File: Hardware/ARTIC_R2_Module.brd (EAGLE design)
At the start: 20.3 x 33 mm, 144 parts, among them J25 U.FL, K1 TLP3475R, Q2 5.8A/30V/35mΩ, U1 ADM4210-1, U2 1.8V/100mA, U3 ARTIC_R2, U4 RFPA0133, U5 AS179-92LF, U6 3.0V, X1 CRYSTAL-TCXO-26MHZ

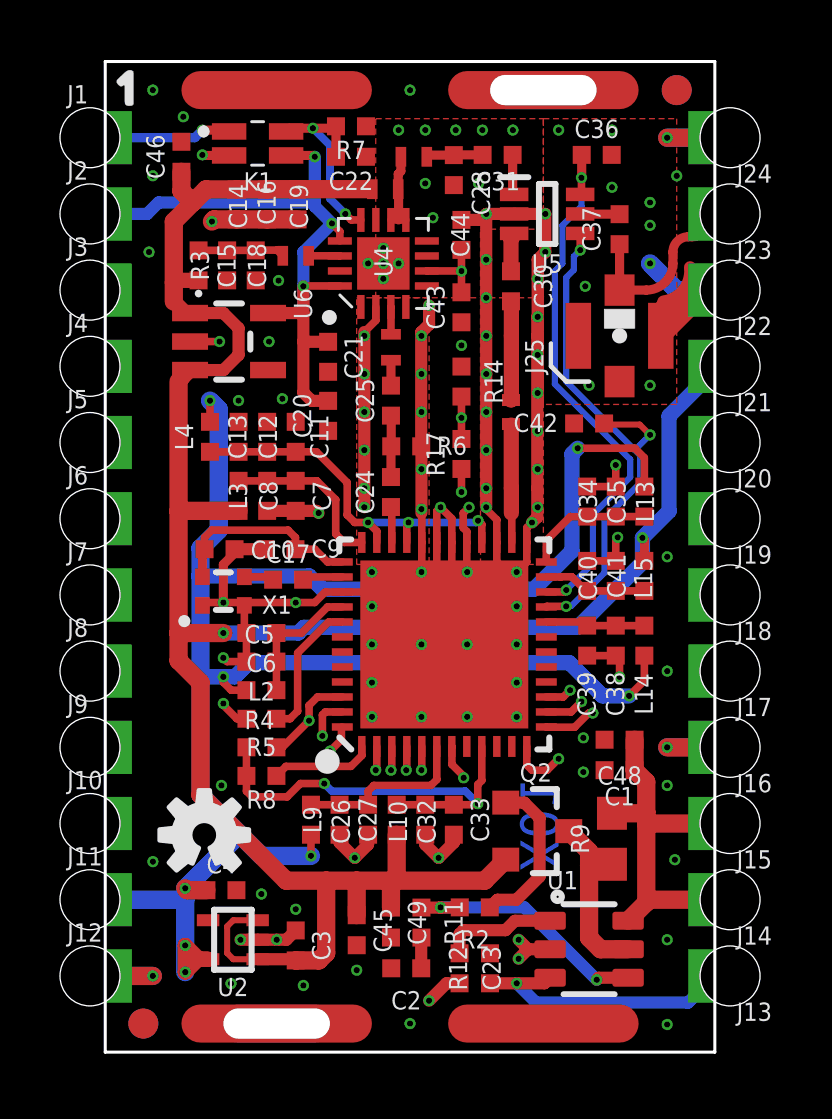
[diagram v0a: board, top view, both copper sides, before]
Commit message: Added the flash memory in USON format
The flash has its own power pin so it can be programmed independantly - without needing the ARTIC to be powered up and held in reset. The user will need to jump the flash power pad across to the adjacent VDD pad on their board.
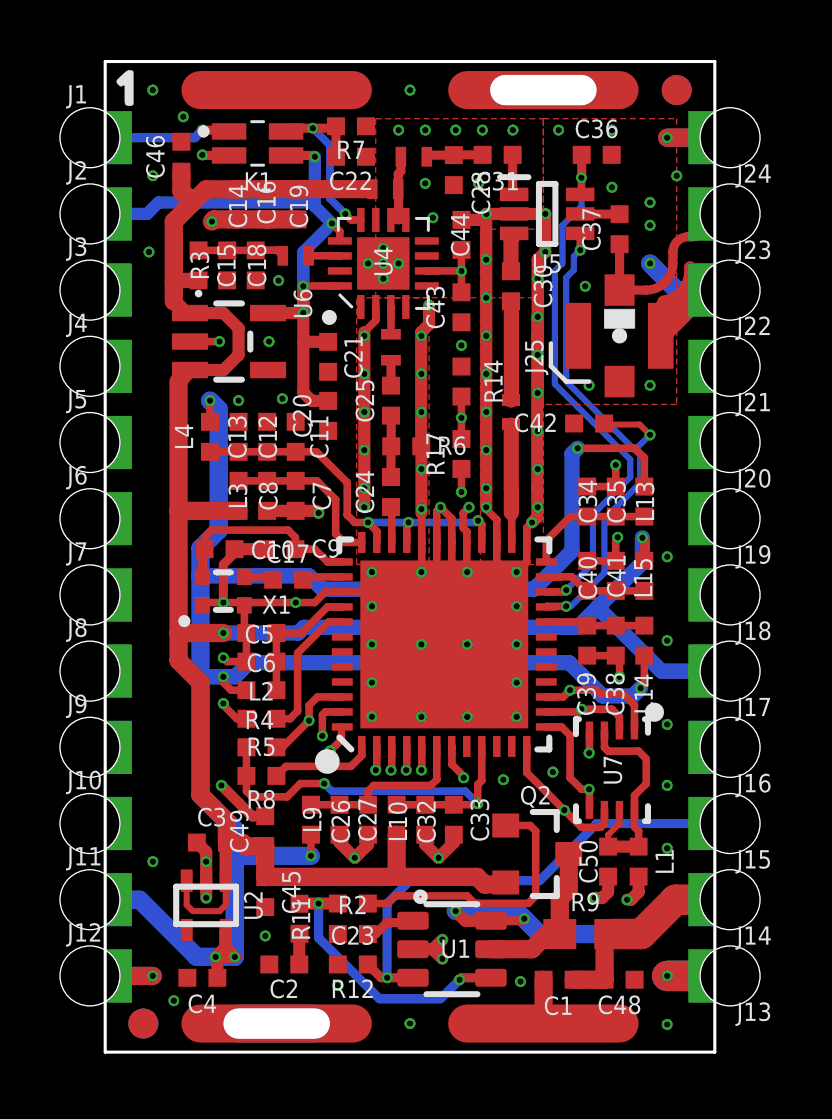
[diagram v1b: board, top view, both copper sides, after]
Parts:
- removed LOGO2: OSHW-LOGOS, SparkFun-Aesthetics:OSHW-LOGO-S
- added C50: 0.1uF, SparkFun-Capacitors:0402-TIGHT
- added L1: 30Ω, SparkFun-Coils:0402-TIGHT
- added U7: SST25VF020BUSON, New_Parts_IC-Memory:USON_3X2MM
- U$8: device output:#VIN#0 -> output:#FLASH_PWR#0
- moved U$13 10.2 mm to (15.7, 12.7)
- moved C48 8.00 mm to (17.1, 2.41), turned to 0 degrees
- moved U$4 7.62 mm to (17.4, 2.54)
- moved C1 7.27 mm to (15.1, 2.41)
- moved U$8 5.34 mm to (16.0, 10.2)
- moved C49 5.18 mm to (5.33, 7.37), turned to 90 degrees
- moved U$6 5.08 mm to (16.3, 7.62)
- moved R12 4.57 mm to (8.26, 2.92), turned to 180 degrees
- moved U1 4.57 mm to (11.6, 3.43)
- moved C3 4.42 mm to (3.56, 6.99), turned to 180 degrees
- moved R11 4.07 mm to (6.48, 4.45)
- moved R2 4.07 mm to (8.26, 4.95)
- moved C2 4.07 mm to (5.97, 2.92)
- moved C23 3.74 mm to (8.26, 3.94), turned to 180 degrees
- moved C45 3.30 mm to (5.33, 5.33)
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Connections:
- new net FLASH_PWR: J16.1, L1.2
- new net FLASH_VCC: C50.1, L1.1, U7.3, U7.7, U7.8
- net FLSH_CEN: now also J21.1, U7.1; no longer J20.1
- net FLSH_SCLK: now also J18.1, U7.6; no longer J17.1
- net FLSH_SI: now also J19.1, U7.5; no longer J18.1
- net FLSH_SO: now also J20.1, U7.2; no longer J19.1
- net GND: now also C50.2, J13.1, U7.4; no longer J16.1
- net PWR_EN: now also J15.1; no longer J13.1
- net VDD: now also J17.1; no longer J21.1
- net VIN: no longer J15.1
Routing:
- net FLASH_PWR: track 0.00 -> 8.41 mm, vias 0 -> 1
- net FLSH_SCLK: track 8.33 -> 16.5 mm
- net FLASH_VCC: track 0.00 -> 7.66 mm
- net VDD: track 81.7 -> 74.9 mm
- net PWR_EN: track 9.32 -> 16.2 mm
- net VIN: track 12.2 -> 18.5 mm, vias 0 -> 2
- net FLSH_SI: track 9.16 -> 15.2 mm
- net FLSH_CEN: track 12.5 -> 17.3 mm
- net GND: track 117.5 -> 121.3 mm
- net N$2: track 5.38 -> 9.14 mm
- net FLSH_SO: track 11.5 -> 14.7 mm
- net N$7: track 3.84 -> 1.69 mm
- net 1.8V: track 68.5 -> 69.4 mm, vias 8 -> 7
- net N$1: track 6.07 -> 5.30 mm
- net N$3: track 8.57 -> 9.30 mm
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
